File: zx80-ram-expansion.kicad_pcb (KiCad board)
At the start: 2 copper layers, 33 x 62 mm, 3 parts, among them J1 Conn_02x23_Odd_Even, U1 74LS00, U2 KM62256CLP

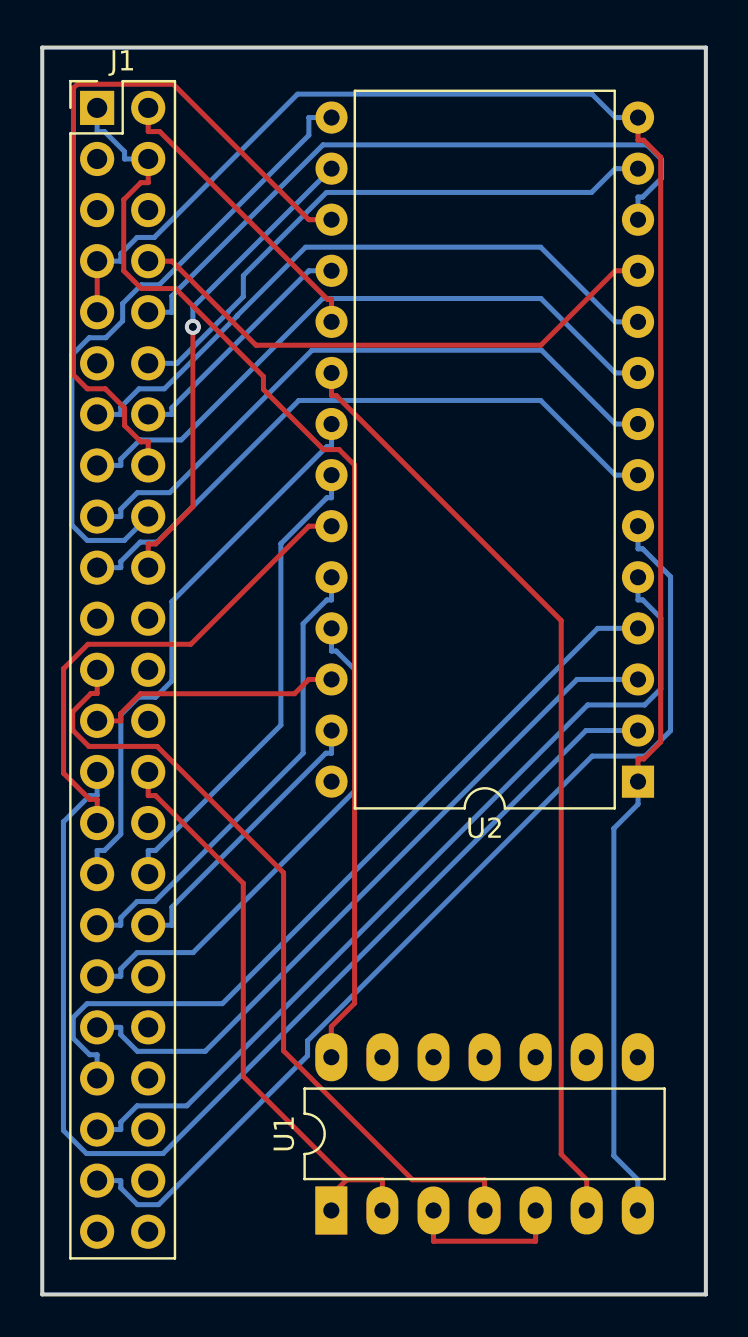
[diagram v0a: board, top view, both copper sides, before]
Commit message: small correction, remove via hole
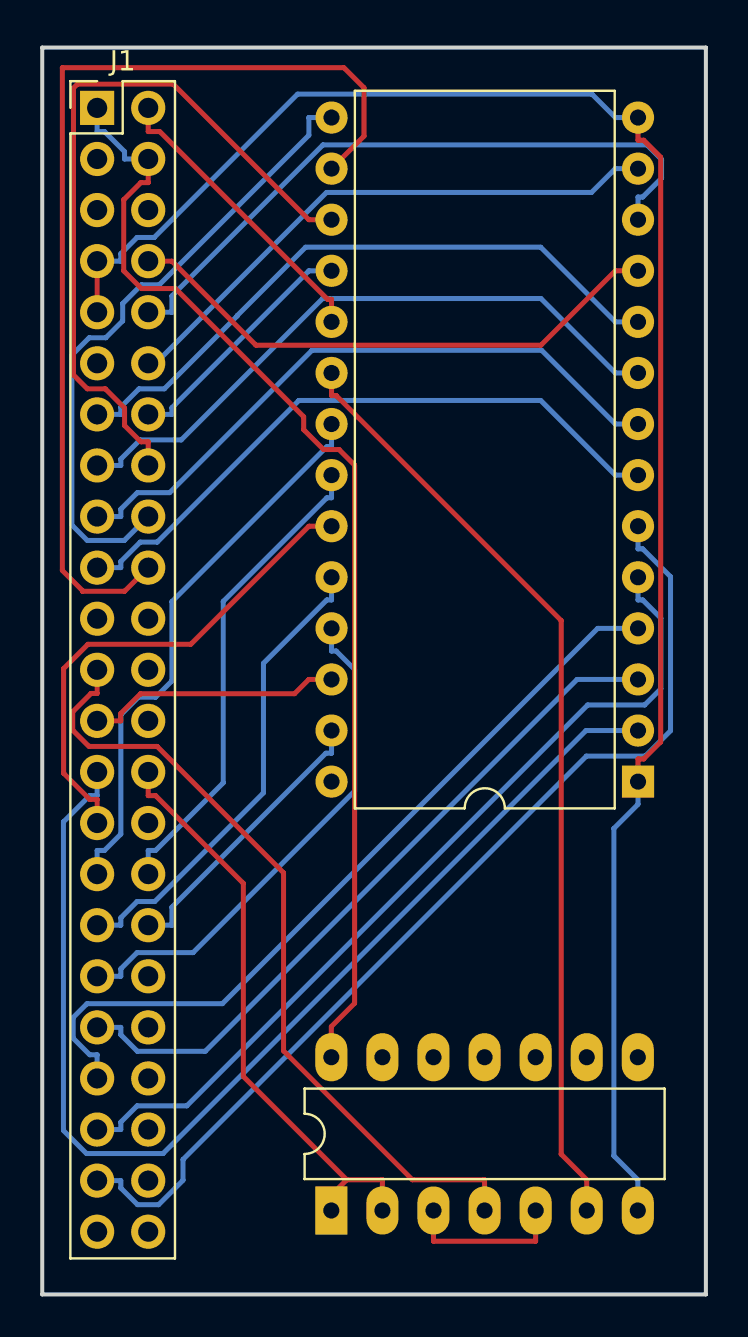
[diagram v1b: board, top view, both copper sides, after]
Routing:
- net D4: track 23.8 -> 50.3 mm, vias 1 -> 0
- net D2: track 29.0 -> 28.4 mm
- added copper zone on B.Cu, net GND
- added copper zone on F.Cu, net GND
